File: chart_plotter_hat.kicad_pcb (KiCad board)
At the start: 4 copper layers, 65 x 56 mm, 65 parts, among them J1 JST PH, J10 JST PH, J2 JST PH, J3 40HAT, J4 JST PH, J5 JST PH, J6 JST PH, J7 JST PH, J8 Conn_02x03_Odd_Even, J9 JST PH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

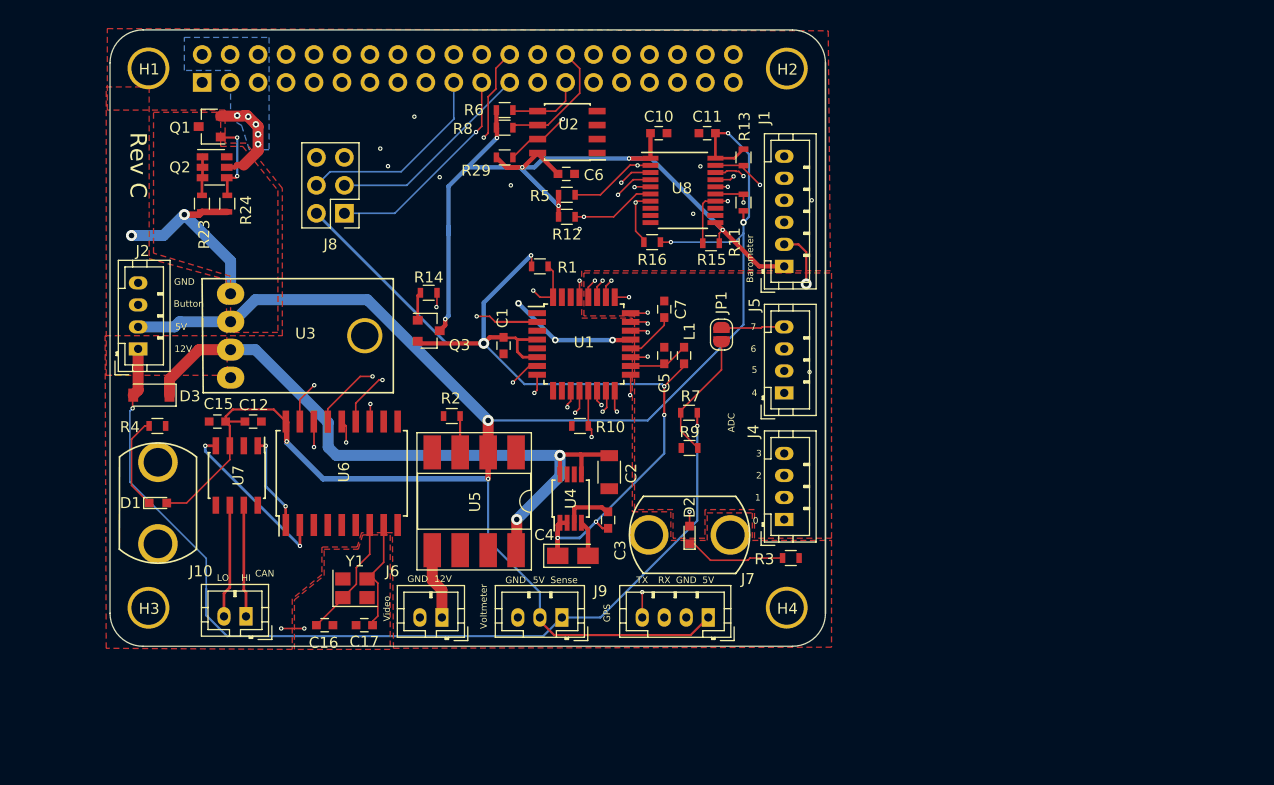
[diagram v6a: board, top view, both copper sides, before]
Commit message: Added optical isolation in CAN
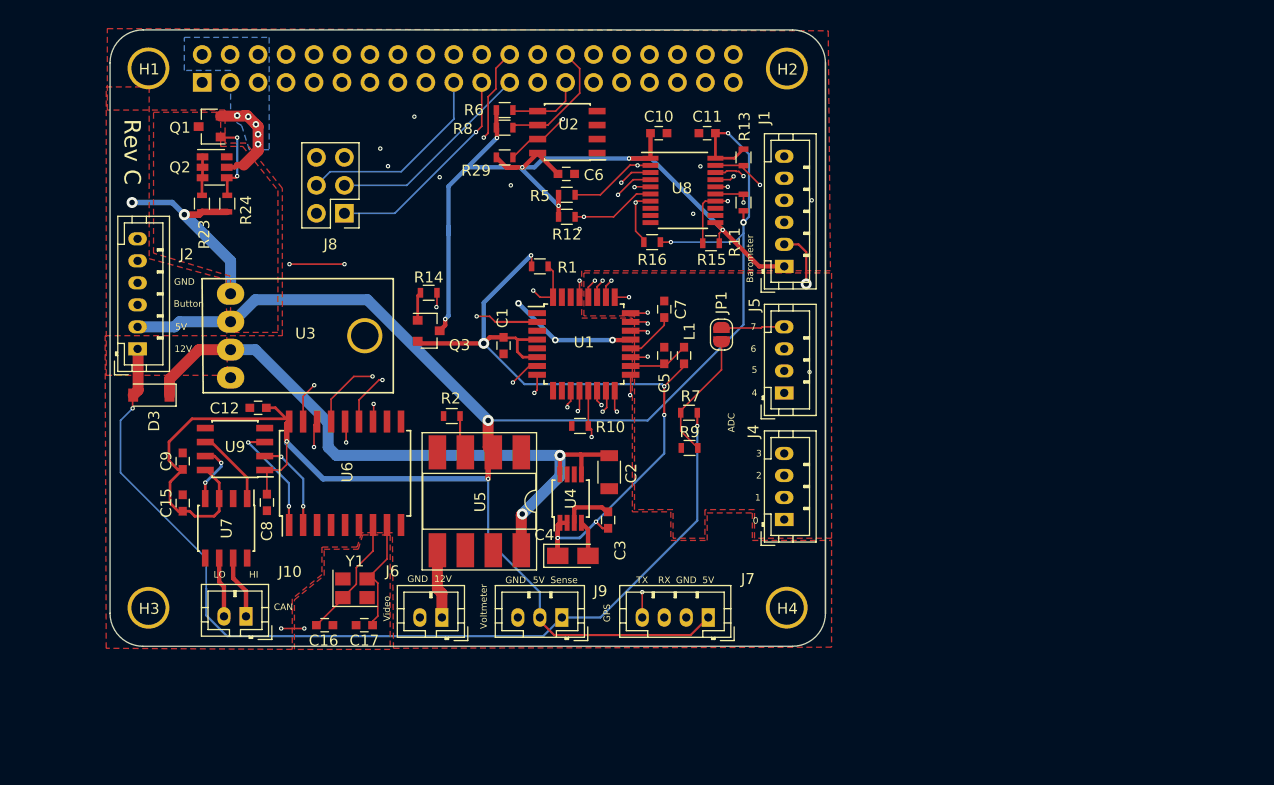
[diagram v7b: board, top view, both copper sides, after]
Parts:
- removed D1, D2: LED, LEDs:LED_0603
- removed H5, H6: LightPipeMount, project_footprints:SMFLPX.X-light-pipe-adapter-smd
- removed R3: 120, Resistors_SMD:R_0603
- removed R4: 300, Resistors_SMD:R_0603
- added C8: .1uF, Capacitors_SMD:C_0603, F.Cu at (92.8, 103.8)
- added C9: .1uF, Capacitors_SMD:C_0603, F.Cu at (85.2, 100.0)
- added U9: ADuM1201BR, Housings_SOIC:SOIC-8_3.9x4.9mm_Pitch1.27mm, F.Cu at (89.9, 98.9)
- J2: footprint Connectors_JST:JST_PH_B4B-PH-K_04x2.00mm_Straight -> Connectors_JST:JST_PH_B6B-PH-K_06x2.00mm_Straight
- moved C15 8.04 mm to (85.2, 103.8), turned to 90 degrees
- moved U7 4.90 mm to (89.1, 106.1)
- moved C12 1.33 mm to (92.0, 95.2), turned to 180 degrees
- moved U5 0.47 mm to (112.1, 103.6)
- moved U6 0.30 mm to (99.9, 101.1)
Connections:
- J2 pad 4: GND -> +5V
- J8 pad 2: +3V3 -> (no net)
- U1 pad 12: Net-(D2-Pad2) -> LED_ACTION
- U7 pad 1: Net-(U6-Pad1) -> Net-(U7-Pad1)
- U7 pad 4: Net-(U6-Pad2) -> Net-(U7-Pad4)
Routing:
- net LED_ACTION: track 0.00 -> 47.7 mm, vias 0 -> 3
- net Net-(D2-Pad2): track 18.8 -> 0.00 mm, vias 2 -> 0
- net +5V: track 175.4 -> 193.9 mm
- net +3V3: track 91.8 -> 75.1 mm
- net Net-(D2-Pad1): track 9.15 -> 0.00 mm
- net Net-(D1-Pad1): track 8.56 -> 0.00 mm
- net Net-(U7-Pad1): track 0.00 -> 7.04 mm
- net Net-(U6-Pad2): track 15.5 -> 8.56 mm
- net Net-(U7-Pad4): track 0.00 -> 5.56 mm, vias 0 -> 2
- net CAN_LO: track 10.3 -> 5.48 mm
- net CAN_HI: track 10.2 -> 5.78 mm
- net Net-(U6-Pad1): track 8.68 -> 10.6 mm
- net /12VBAT: track 86.9 -> 87.6 mm

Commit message: Redid CAN isolation, removed level shifter
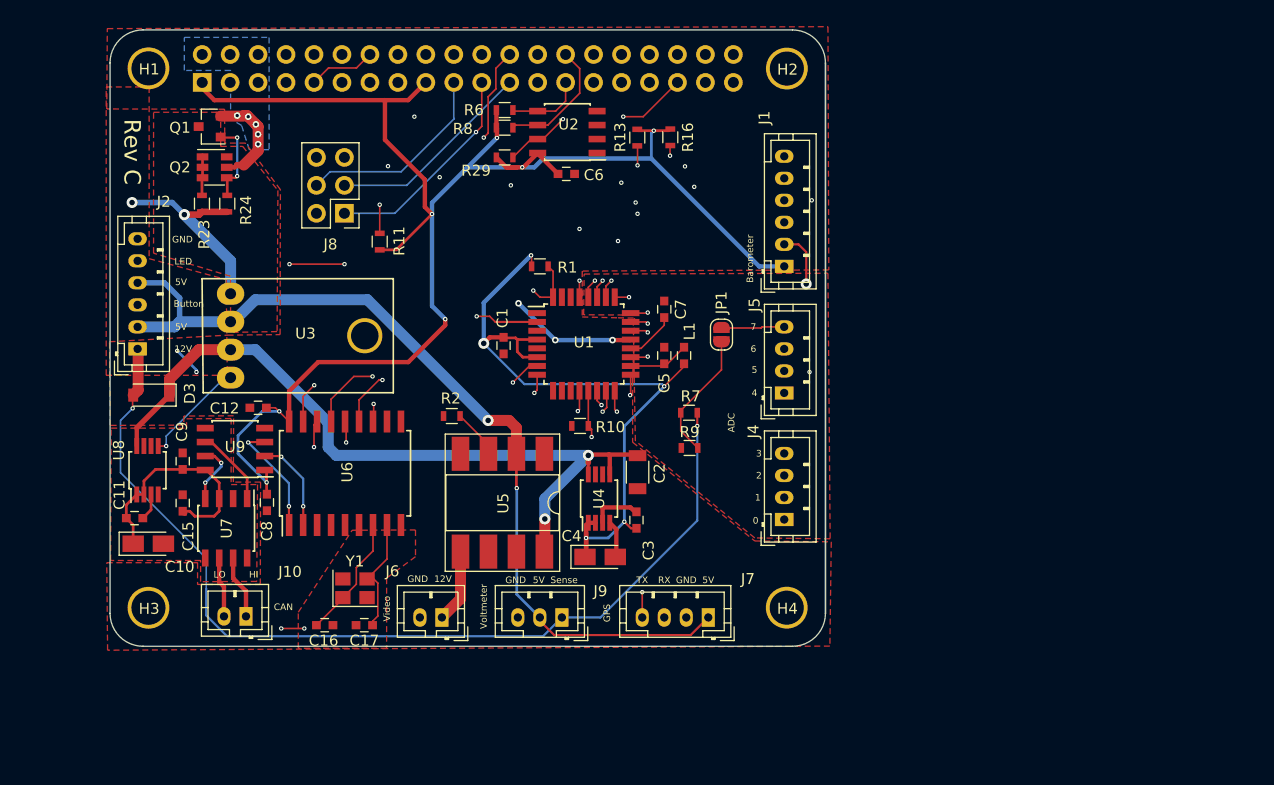
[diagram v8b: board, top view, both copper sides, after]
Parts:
- removed Q3: DMG2305UX, TO_SOT_Packages_SMD:SOT-23
- removed R12, R15, R5: 10K, Resistors_SMD:R_0603
- removed R14: 220, Resistors_SMD:R_0603
- C10: value .1uF -> 10uF; footprint Capacitors_SMD:C_0603 -> Capacitors_Tantalum_SMD:CP_Tantalum_Case-A_EIA-3216-18_Reflow
- C11: value .1uF -> .01uF
- U8: value ST2378E -> LT1762-MS8; footprint Housings_SSOP:TSSOP-20_4.4x6.5mm_Pitch0.65mm -> Housings_SSOP:MSOP-8_3x3mm_Pitch0.65mm
- moved C11 62.7 mm to (80.8, 105.2)
- moved C10 59.5 mm to (82.0, 107.5), turned to 0 degrees
- moved U8 54.9 mm to (82.0, 100.8), turned to 90 degrees
- moved R11 33.2 mm to (103.0, 80.0)
- moved R13 9.82 mm to (126.5, 70.6)
- moved R16 9.67 mm to (129.4, 70.6), turned to 90 degrees
- moved C3 2.58 mm to (126.4, 105.3)
- moved C2 2.57 mm to (126.5, 101.0)
- moved U4 2.57 mm to (123.0, 103.4)
- moved C4 2.48 mm to (123.1, 108.7)
- moved U5 2.10 mm to (114.2, 103.8)
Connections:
- C10 pad 1: GND -> +5VP
- C10 pad 2: VEE -> GND2
- C11 pad 1: GND -> +5VP
- C11 pad 2: +5V -> Net-(C11-Pad2)
- C12 pad 1: +5V -> VEE
- C15 pad 1: +5V -> +5VP
- C15 pad 2: GND -> GND2
- C8 pad 1: +5V -> VEE
- C9 pad 1: +5V -> +5VP
- C9 pad 2: GND -> GND2
- J3 pad 1: (no net) -> VEE
- J3 pad 17: (no net) -> VEE
- J3 pad 35: MISO-2 -> CAN_SO
- J3 pad 38: MOSI-2 -> CAN_SI
- J3 pad 40: SCK-2 -> CAN_SCK
- R11 pad 1: CCS -> CAN_CS
- R11 pad 2: +5V -> VEE
- R13 pad 1: +5V -> VEE
- R13 pad 2: INT -> CAN_INT
- R16 pad 1: CRST -> CAN_RST
- R16 pad 2: +5V -> VEE
- U1 pad 11: VEE_ENABLE -> (no net)
- U6 pad 12: INT -> CAN_INT
- U6 pad 16: CCS -> CAN_CS
- U6 pad 17: CRST -> CAN_RST
- U6 pad 18: +5V -> VEE
- U7 pad 2: GND -> GND2
- U7 pad 3: +5V -> +5VP
- U7 pad 8: GND -> GND2
- U8 pad 1: VEE -> +5VP
- U8 pad 2: CAN_INT -> +5VP
- U8 pad 3: CAN_SO -> Net-(C11-Pad2)
- U8 pad 4: MOSI-2 -> GND2
- U8 pad 5: CAN_SCK -> EN
- U8 pad 6: CAN_CS -> (no net)
- U8 pad 7: CRST -> GND2
- U8 pad 8: (no net) -> +12V
- U9 pad 1: +5V -> VEE
- U9 pad 5: GND -> GND2
- U9 pad 8: +5V -> +5VP
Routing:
- net +5V: track 193.9 -> 81.7 mm, vias 6 -> 2
- net VEE: track 78.2 -> 143.7 mm, vias 6 -> 7
- net CCS: track 54.0 -> 0.00 mm, vias 2 -> 0
- net INT: track 52.6 -> 0.00 mm, vias 3 -> 0
- net CRST: track 45.3 -> 0.00 mm, vias 2 -> 0
- net CAN_RST: track 22.3 -> 56.4 mm, vias 1 -> 3
- net MOSI-2: track 26.6 -> 0.00 mm, vias 1 -> 0
- net CAN_INT: track 31.8 -> 53.7 mm, vias 2 -> 4
- net +5VP: track 0.00 -> 21.3 mm
- net VEE_ENABLE: track 19.3 -> 0.00 mm, vias 2 -> 0
- net CAN_SCK: track 38.0 -> 55.4 mm
- net MISO-2: track 17.4 -> 0.00 mm, vias 1 -> 0
- net SCK-2: track 17.3 -> 0.00 mm, vias 1 -> 0
- net CAN_SI: track 50.8 -> 61.8 mm
- net +3V3: track 75.1 -> 64.5 mm, vias 6 -> 5
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- added copper zone on F.Cu, net GND2
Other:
- board text added: "LED"
